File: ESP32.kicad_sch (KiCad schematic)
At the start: 1 part, among them U1 ESP32-S3-MINI-1

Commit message: add ADC circuit, a few more DNP components, and assigned footprints
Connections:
- net LED3: now reaches U1.14 (GPIO10/TOUCH10/ADC1_CH9/FSPICS0/FSPIIO4/SUBSPICS0)
- net LED4: now reaches U1.15 (GPIO11/TOUCH11/ADC2_CH0/FSPID/FSPIIO5/SUBSPID)
- net LED5: now reaches U1.16 (GPIO12/TOUCH12/ADC2_CH1/FSPICLK/FSPIIO6/SUBSPICLK)
- net VBAT_ADC_EN: now reaches U1.17 (GPIO13/TOUCH13/ADC2_CH2/FSPIQ/FSPIIO7/SUBSPIQ)
- net VBAT_ADC: now reaches U1.5 (GPIO1/TOUCH1/ADC1_CH0)
- no-connect marks 0 -> 23
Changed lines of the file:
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@@
     (company "J2B")
   )
+  (no_connect (at 193.04 113.03))
+  (no_connect (at 193.04 82.55))
+  (no_connect (at 193.04 85.09))
+  (no_connect (at 101.6 123.19))
+  (no_connect (at 193.04 120.65))
+  (no_connect (at 101.6 133.35))
+  (no_connect (at 193.04 123.19))
+  (no_connect (at 193.04 130.81))
+  (no_connect (at 101.6 120.65))
+  (no_connect (at 193.04 115.57))
+  (no_connect (at 193.04 125.73))
+  (no_connect (at 101.6 128.27))
+  (no_connect (at 193.04 133.35))
+  (no_connect (at 193.04 72.39))
+  (no_connect (at 101.6 130.81))
+  (no_connect (at 101.6 82.55))
+  (no_connect (at 101.6 77.47))
+  (no_connect (at 193.04 69.85))
+  (no_connect (at 101.6 80.01))
+  (no_connect (at 101.6 74.93))
+  (no_connect (at 193.04 118.11))
+  (no_connect (at 101.6 125.73))
+  (no_connect (at 193.04 128.27))
   (wire (pts (xy 193.04 95.25) (xy 198.12 95.25))
+    (stroke (width 0) (type default))
+  )
+  (wire (pts (xy 193.04 80.01) (xy 198.12 80.01))
     (stroke (width 0) (type default))
   )
@@
   )
   (wire (pts (xy 193.04 64.77) (xy 198.12 64.77))
+    (stroke (width 0) (type default))
+  )
+  (wire (pts (xy 193.04 105.41) (xy 198.12 105.41))
     (stroke (width 0) (type default))
   )
@@
     (stroke (width 0) (type default))
   )
+  (wire (pts (xy 193.04 110.49) (xy 198.12 110.49))
+    (stroke (width 0) (type default))
+  )
   (wire (pts (xy 96.52 62.23) (xy 101.6 62.23))
     (stroke (width 0) (type default))
   )
   (wire (pts (xy 147.32 138.43) (xy 147.32 143.51))
+    (stroke (width 0) (type default))
+  )
+  (wire (pts (xy 193.04 107.95) (xy 198.12 107.95))
+    (stroke (width 0) (type default))
+  )
+  (wire (pts (xy 193.04 102.87) (xy 198.12 102.87))
     (stroke (width 0) (type default))
   )
@@
   )
   (hierarchical_label "UNLOCK" (shape input) (at 198.12 92.71 0) (fields_autoplaced)
+    (effects (font (size 1.27 1.27)) (justify left))
+  )
+  (hierarchical_label "VBAT_ADC" (shape input) (at 198.12 80.01 0) (fields_autoplaced)
     (effects (font (size 1.27 1.27)) (justify left))
   )
@@
   )
   (hierarchical_label "VCC" (shape input) (at 147.32 52.07 90) (fields_autoplaced)
+    (effects (font (size 1.27 1.27)) (justify left))
+  )
+  (hierarchical_label "LED4" (shape output) (at 198.12 105.41 0) (fields_autoplaced)
     (effects (font (size 1.27 1.27)) (justify left))
   )
@@
     (effects (font (size 1.27 1.27)) (justify left))
   )
+  (hierarchical_label "LED3" (shape output) (at 198.12 102.87 0) (fields_autoplaced)
+    (effects (font (size 1.27 1.27)) (justify left))
+  )
+  (hierarchical_label "VBAT_ADC_EN" (shape output) (at 198.12 110.49 0) (fields_autoplaced)
+    (effects (font (size 1.27 1.27)) (justify left))
+  )
+  (hierarchical_label "LED5" (shape output) (at 198.12 107.95 0) (fields_autoplaced)
+    (effects (font (size 1.27 1.27)) (justify left))
+  )

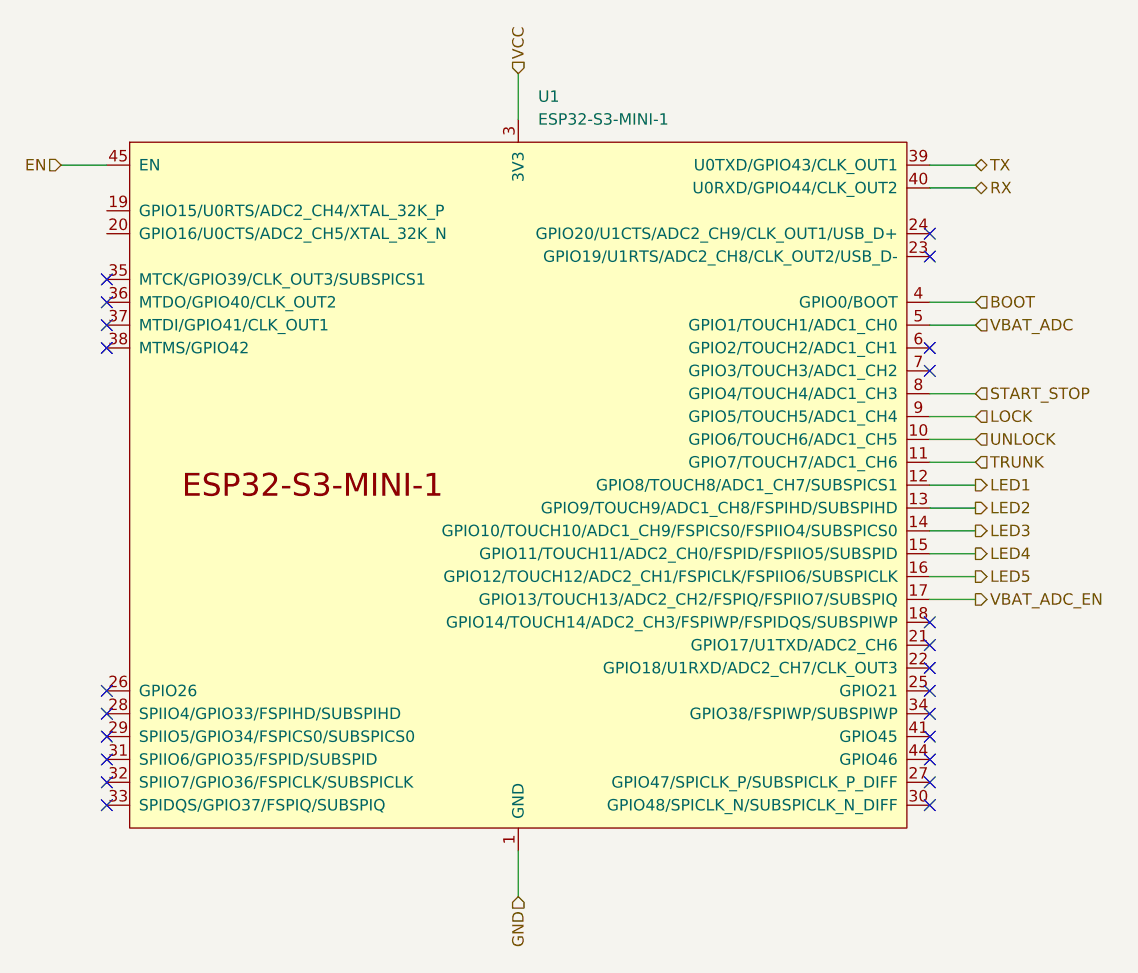
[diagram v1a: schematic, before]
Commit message: create libraries folder for sharing external libs
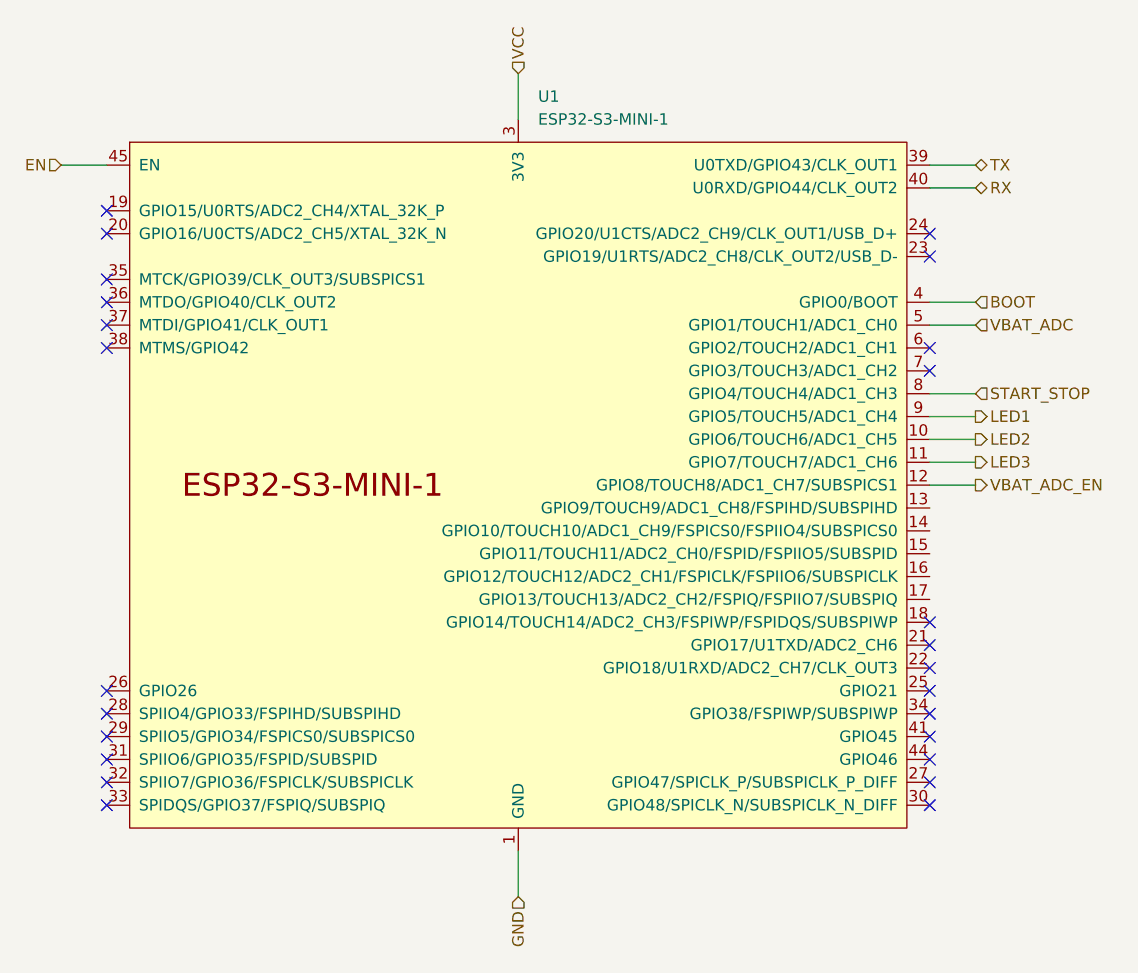
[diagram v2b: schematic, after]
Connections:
- net LOCK is gone; now on net LED1: U1.9 (GPIO5/TOUCH5/ADC1_CH4)
- net TRUNK is gone; now on net LED3: U1.11 (GPIO7/TOUCH7/ADC1_CH6)
- net UNLOCK is gone; now on net LED2: U1.10 (GPIO6/TOUCH6/ADC1_CH5)
- net LED1: no longer U1.12 (GPIO8/TOUCH8/ADC1_CH7/SUBSPICS1)
- net LED2: no longer U1.13 (GPIO9/TOUCH9/ADC1_CH8/FSPIHD/SUBSPIHD)
- net LED3: no longer U1.14 (GPIO10/TOUCH10/ADC1_CH9/FSPICS0/FSPIIO4/SUBSPICS0)
- net VBAT_ADC_EN: now also U1.12 (GPIO8/TOUCH8/ADC1_CH7/SUBSPICS1); no longer U1.17 (GPIO13/TOUCH13/ADC2_CH2/FSPIQ/FSPIIO7/SUBSPIQ)
- net LED4: no longer names the net of U1.15 (GPIO11/TOUCH11/ADC2_CH0/FSPID/FSPIIO5/SUBSPID)
- net LED5: no longer names the net of U1.16 (GPIO12/TOUCH12/ADC2_CH1/FSPICLK/FSPIIO6/SUBSPICLK)
- no-connect marks 23 -> 25
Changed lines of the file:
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@@
   (no_connect (at 101.6 77.47))
   (no_connect (at 193.04 69.85))
+  (no_connect (at 101.6 67.31))
   (no_connect (at 101.6 80.01))
   (no_connect (at 101.6 74.93))
   (no_connect (at 193.04 118.11))
   (no_connect (at 101.6 125.73))
+  (no_connect (at 101.6 69.85))
   (no_connect (at 193.04 128.27))
-  (wire (pts (xy 193.04 95.25) (xy 198.12 95.25))
-    (stroke (width 0) (type default))
-  )
   (wire (pts (xy 193.04 80.01) (xy 198.12 80.01))
-    (stroke (width 0) (type default))
-  )
-  (wire (pts (xy 193.04 92.71) (xy 198.12 92.71))
     (stroke (width 0) (type default))
   )
@@
     (stroke (width 0) (type default))
   )
-  (wire (pts (xy 193.04 105.41) (xy 198.12 105.41))
+  (wire (pts (xy 193.04 95.25) (xy 198.12 95.25))
     (stroke (width 0) (type default))
   )
   (wire (pts (xy 193.04 62.23) (xy 198.12 62.23))
+    (stroke (width 0) (type default))
+  )
+  (wire (pts (xy 193.04 97.79) (xy 198.12 97.79))
+    (stroke (width 0) (type default))
+  )
+  (wire (pts (xy 193.04 90.17) (xy 198.12 90.17))
     (stroke (width 0) (type default))
   )
@@
     (stroke (width 0) (type default))
   )
-  (wire (pts (xy 193.04 100.33) (xy 198.12 100.33))
-    (stroke (width 0) (type default))
-  )
-  (wire (pts (xy 193.04 110.49) (xy 198.12 110.49))
-    (stroke (width 0) (type default))
-  )
   (wire (pts (xy 96.52 62.23) (xy 101.6 62.23))
     (stroke (width 0) (type default))
@@
     (stroke (width 0) (type default))
   )
-  (wire (pts (xy 193.04 107.95) (xy 198.12 107.95))
+  (wire (pts (xy 193.04 92.71) (xy 198.12 92.71))
     (stroke (width 0) (type default))
-  )
-  (wire (pts (xy 193.04 102.87) (xy 198.12 102.87))
-    (stroke (width 0) (type default))
-  )
-  (wire (pts (xy 193.04 90.17) (xy 198.12 90.17))
-    (stroke (width 0) (type default))
-  )
-  (wire (pts (xy 193.04 97.79) (xy 198.12 97.79))
-    (stroke (width 0) (type default))
-  )
-  (hierarchical_label "UNLOCK" (shape input) (at 198.12 92.71 0) (fields_autoplaced)
-    (effects (font (size 1.27 1.27)) (justify left))
   )
   (hierarchical_label "VBAT_ADC" (shape input) (at 198.12 80.01 0) (fields_autoplaced)
@@
     (effects (font (size 1.27 1.27)) (justify left))
   )
-  (hierarchical_label "TRUNK" (shape input) (at 198.12 95.25 0) (fields_autoplaced)
-    (effects (font (size 1.27 1.27)) (justify left))
-  )
-  (hierarchical_label "LOCK" (shape input) (at 198.12 90.17 0) (fields_autoplaced)
-    (effects (font (size 1.27 1.27)) (justify left))
-  )
   (hierarchical_label "VCC" (shape input) (at 147.32 52.07 90) (fields_autoplaced)
     (effects (font (size 1.27 1.27)) (justify left))
   )
-  (hierarchical_label "LED4" (shape output) (at 198.12 105.41 0) (fields_autoplaced)
-    (effects (font (size 1.27 1.27)) (justify left))
-  )
-  (hierarchical_label "LED2" (shape output) (at 198.12 100.33 0) (fields_autoplaced)
+  (hierarchical_label "LED2" (shape output) (at 198.12 92.71 0) (fields_autoplaced)
     (effects (font (size 1.27 1.27)) (justify left))
   )
@@
     (effects (font (size 1.27 1.27)) (justify right))
   )
-  (hierarchical_label "LED1" (shape output) (at 198.12 97.79 0) (fields_autoplaced)
+  (hierarchical_label "LED1" (shape output) (at 198.12 90.17 0) (fields_autoplaced)
     (effects (font (size 1.27 1.27)) (justify left))
   )
-  (hierarchical_label "LED3" (shape output) (at 198.12 102.87 0) (fields_autoplaced)
+  (hierarchical_label "LED3" (shape output) (at 198.12 95.25 0) (fields_autoplaced)
     (effects (font (size 1.27 1.27)) (justify left))
   )
-  (hierarchical_label "VBAT_ADC_EN" (shape output) (at 198.12 110.49 0) (fields_autoplaced)
+  (hierarchical_label "VBAT_ADC_EN" (shape output) (at 198.12 97.79 0) (fields_autoplaced)
     (effects (font (size 1.27 1.27)) (justify left))
   )
-  (hierarchical_label "LED5" (shape output) (at 198.12 107.95 0) (fields_autoplaced)
-    (effects (font (size 1.27 1.27)) (justify left))
-  )

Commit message: inital layout of components complete
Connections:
- no-connect marks 25 -> 30
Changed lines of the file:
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@@
   (no_connect (at 193.04 113.03))
   (no_connect (at 193.04 82.55))
+  (no_connect (at 193.04 100.33))
   (no_connect (at 193.04 85.09))
   (no_connect (at 101.6 123.19))
+  (no_connect (at 193.04 107.95))
   (no_connect (at 193.04 120.65))
   (no_connect (at 101.6 133.35))
@@
   (no_connect (at 101.6 77.47))
   (no_connect (at 193.04 69.85))
+  (no_connect (at 193.04 110.49))
   (no_connect (at 101.6 67.31))
+  (no_connect (at 193.04 102.87))
   (no_connect (at 101.6 80.01))
+  (no_connect (at 193.04 105.41))
   (no_connect (at 101.6 74.93))
   (no_connect (at 193.04 118.11))

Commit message: layout complete
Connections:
- net LED1: now also U1.16 (GPIO12/TOUCH12/ADC2_CH1/FSPICLK/FSPIIO6/SUBSPICLK); no longer U1.9 (GPIO5/TOUCH5/ADC1_CH4)
- net LED2: now also U1.17 (GPIO13/TOUCH13/ADC2_CH2/FSPIQ/FSPIIO7/SUBSPIQ); no longer U1.10 (GPIO6/TOUCH6/ADC1_CH5)
- net LED3: now also U1.18 (GPIO14/TOUCH14/ADC2_CH3/FSPIWP/FSPIDQS/SUBSPIWP); no longer U1.11 (GPIO7/TOUCH7/ADC1_CH6)
- net START_STOP: now also U1.21 (GPIO17/U1TXD/ADC2_CH6); no longer U1.8 (GPIO4/TOUCH4/ADC1_CH3)
- net VBAT_ADC_EN: now also U1.11 (GPIO7/TOUCH7/ADC1_CH6); no longer U1.12 (GPIO8/TOUCH8/ADC1_CH7/SUBSPICS1)
- no-connect marks 30 -> 24
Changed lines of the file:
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@@
     (company "J2B")
   )
-  (no_connect (at 193.04 113.03))
-  (no_connect (at 193.04 82.55))
   (no_connect (at 193.04 100.33))
   (no_connect (at 193.04 85.09))
   (no_connect (at 101.6 123.19))
-  (no_connect (at 193.04 107.95))
   (no_connect (at 193.04 120.65))
   (no_connect (at 101.6 133.35))
@@
   (no_connect (at 193.04 130.81))
   (no_connect (at 101.6 120.65))
-  (no_connect (at 193.04 115.57))
   (no_connect (at 193.04 125.73))
   (no_connect (at 101.6 128.27))
@@
   (no_connect (at 101.6 77.47))
   (no_connect (at 193.04 69.85))
-  (no_connect (at 193.04 110.49))
   (no_connect (at 101.6 67.31))
   (no_connect (at 193.04 102.87))
   (no_connect (at 101.6 80.01))
-  (no_connect (at 193.04 105.41))
   (no_connect (at 101.6 74.93))
   (no_connect (at 193.04 118.11))
@@
     (stroke (width 0) (type default))
   )
+  (wire (pts (xy 193.04 113.03) (xy 198.12 113.03))
+    (stroke (width 0) (type default))
+  )
   (wire (pts (xy 193.04 64.77) (xy 198.12 64.77))
+    (stroke (width 0) (type default))
+  )
+  (wire (pts (xy 193.04 62.23) (xy 198.12 62.23))
+    (stroke (width 0) (type default))
+  )
+  (wire (pts (xy 193.04 107.95) (xy 198.12 107.95))
+    (stroke (width 0) (type default))
+  )
+  (wire (pts (xy 193.04 77.47) (xy 198.12 77.47))
     (stroke (width 0) (type default))
   )
@@
     (stroke (width 0) (type default))
   )
-  (wire (pts (xy 193.04 62.23) (xy 198.12 62.23))
-    (stroke (width 0) (type default))
-  )
-  (wire (pts (xy 193.04 97.79) (xy 198.12 97.79))
-    (stroke (width 0) (type default))
-  )
-  (wire (pts (xy 193.04 90.17) (xy 198.12 90.17))
-    (stroke (width 0) (type default))
-  )
-  (wire (pts (xy 193.04 87.63) (xy 198.12 87.63))
-    (stroke (width 0) (type default))
-  )
-  (wire (pts (xy 193.04 77.47) (xy 198.12 77.47))
+  (wire (pts (xy 193.04 115.57) (xy 198.12 115.57))
     (stroke (width 0) (type default))
   )
   (wire (pts (xy 147.32 52.07) (xy 147.32 57.15))
+    (stroke (width 0) (type default))
+  )
+  (wire (pts (xy 193.04 110.49) (xy 198.12 110.49))
     (stroke (width 0) (type default))
   )
@@
   )
   (wire (pts (xy 147.32 138.43) (xy 147.32 143.51))
-    (stroke (width 0) (type default))
-  )
-  (wire (pts (xy 193.04 92.71) (xy 198.12 92.71))
     (stroke (width 0) (type default))
   )
@@
     (effects (font (size 1.27 1.27)) (justify left))
   )
-  (hierarchical_label "LED2" (shape output) (at 198.12 92.71 0) (fields_autoplaced)
+  (hierarchical_label "LED2" (shape output) (at 198.12 110.49 0) (fields_autoplaced)
     (effects (font (size 1.27 1.27)) (justify left))
   )
@@
     (effects (font (size 1.27 1.27)) (justify left))
   )
-  (hierarchical_label "START_STOP" (shape input) (at 198.12 87.63 0) (fields_autoplaced)
+  (hierarchical_label "START_STOP" (shape input) (at 198.12 115.57 0) (fields_autoplaced)
     (effects (font (size 1.27 1.27)) (justify left))
   )
@@
     (effects (font (size 1.27 1.27)) (justify right))
   )
-  (hierarchical_label "LED1" (shape output) (at 198.12 90.17 0) (fields_autoplaced)
+  (hierarchical_label "LED1" (shape output) (at 198.12 107.95 0) (fields_autoplaced)
     (effects (font (size 1.27 1.27)) (justify left))
   )
-  (hierarchical_label "LED3" (shape output) (at 198.12 95.25 0) (fields_autoplaced)
+  (hierarchical_label "LED3" (shape output) (at 198.12 113.03 0) (fields_autoplaced)
     (effects (font (size 1.27 1.27)) (justify left))
   )
-  (hierarchical_label "VBAT_ADC_EN" (shape output) (at 198.12 97.79 0) (fields_autoplaced)
+  (hierarchical_label "VBAT_ADC_EN" (shape output) (at 198.12 95.25 0) (fields_autoplaced)
     (effects (font (size 1.27 1.27)) (justify left))
   )

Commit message: generate fab files
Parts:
- U1: MPN (none) -> C2913206
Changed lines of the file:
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@@
+      (effects (font (size 1.27 1.27)) hide)
+    )
+    (property "MPN" "C2913206" (at 147.32 97.79 0)
       (effects (font (size 1.27 1.27)) hide)
     )
